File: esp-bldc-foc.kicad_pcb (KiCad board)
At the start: 4 copper layers, 92 x 92 mm, 123 parts, among them IC1 ESP32-S3FN8, IC2 LY68L6400SLIT, IC3 DRV8301DCAR, J1 USB_C_Receptacle_USB2.0, J6 Conn_01x02_Female, J7 A, J8 B, J9 C, Q1 BUK7M9R9-60EX, Q10 BUK7M9R9-60EX, Q11 BUK7M9R9-60EX, Q12 BUK7M9R9-60EX, Q2 BUK7M9R9-60EX, Q3 BUK7M9R9-60EX, Q4 BUK7M9R9-60EX, Q5 BUK7M9R9-60EX, Q6 BUK7M9R9-60EX, Q7 BUK7M9R9-60EX, Q8 BUK7M9R9-60EX, Q9 BUK7M9R9-60EX, SW1 SW_SPST, SW2 SW_SPST, U1 ADP7182AUJZ-3.3, U2 W25Q32JVZP, U3 AS5055A, U4 LMR36510ADDA, U5 LMR36510ADDA, Y1 40MHz

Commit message: finished routing
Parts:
- added J10: UART, Connector_JST:JST_PH_B3B-PH-K_1x03_P2.00mm_Vertical, F.Cu at (133.8, 90.3)
- added J2: ABZ encoder, Connector_JST:JST_PH_B5B-PH-K_1x05_P2.00mm_Vertical, F.Cu at (105.5, 107.1)
- added J3: I2C ENCODER, Connector_JST:JST_PH_B4B-PH-K_1x04_P2.00mm_Vertical, F.Cu at (103.3, 81.8)
- U3: value AS5055A -> AS5048B; footprint Package_DFN_QFN:QFN-16-1EP_4x4mm_P0.65mm_EP2.7x2.7mm_PullBack -> Package_SO:TSSOP-14_4.4x5mm_P0.65mm
- moved R13 11.4 mm to (157.5, 86.3), turned to 90 degrees
- moved C2 1.90 mm to (119.6, 82.2), turned to 0 degrees
- moved C32 1.73 mm to (141.0, 90.8)
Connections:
- IC1 pad 18: /ENC_B -> /ENC_Z
- IC1 pad 19: /ENC_Z -> /ENC_B
- IC1 pad 44: /AS5055_CS -> /ENC_PWM
- U3 pad 1: /ENC_MOSI -> /SDA
- U3 pad 14: unconnected-(U3-Pad14) -> /ENC_PWM
- U3 pad 2: /ENC_MISO -> /SCL
- U3 pad 3: /ENC_SCK -> GND
- U3 pad 4: /AS5055_CS -> GND
- U3 pad 9: GND -> unconnected-(U3-Pad9)
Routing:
- net /SDA: track 0.00 -> 55.9 mm, vias 0 -> 2
- net /SCL: track 0.00 -> 55.0 mm, vias 0 -> 2
- net /MCU/IO4: track 3.96 -> 49.6 mm, vias 0 -> 2
- net /ENC_MISO: track 4.88 -> 37.6 mm, vias 3 -> 2
- net /ENC_SCK: track 2.49 -> 33.7 mm, vias 3 -> 2
- net /MCU/IO10: track 1.94 -> 33.0 mm, vias 2 -> 3
- net /MCU/IO9: track 6.76 -> 36.9 mm
- net /MCU/IO11: track 5.49 -> 35.5 mm
- net /ENC_MOSI: track 3.48 -> 33.4 mm, vias 3 -> 2
- net /ENC_PWM: track 0.00 -> 22.4 mm, vias 0 -> 2
- net /MCU/IO5: track 1.62 -> 21.7 mm, vias 1 -> 3
- net /ENC_Z: track 0.90 -> 20.8 mm
- net /MCU/IO6: track 4.98 -> 23.6 mm, vias 1 -> 2
- net /ENC_A: track 0.71 -> 18.4 mm
- net /ENC_B: track 0.77 -> 18.4 mm
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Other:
- outline, holes or cut-outs redrawn

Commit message: Routing done
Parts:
- removed C1: C, Capacitor_SMD:C_0402_1005Metric
- removed C11: 0.1uF, Capacitor_SMD:C_0402_1005Metric
- removed C13, C15: 2200pF, Capacitor_SMD:C_0402_1005Metric
- removed C27, C39: 100nF, Capacitor_SMD:C_0402_1005Metric
- removed C30: 68uF, Capacitor_Tantalum_SMD:CP_EIA-7361-438_AVX-U_Pad2.18x3.30mm_HandSolder
- removed C31: 2.2uF, Capacitor_SMD:C_0402_1005Metric
- removed C33, C35: 220nF, Capacitor_SMD:C_0402_1005Metric
- removed C37: 1uF, Capacitor_SMD:C_0402_1005Metric
- removed C41: 10pF, Capacitor_SMD:C_0402_1005Metric
- removed C43: 47uF, Capacitor_SMD:C_1206_3216Metric
- removed C45, C48: 470uF, Capacitor_SMD:CP_Elec_10x10
- removed C50, C51: 4.7uF, Capacitor_SMD:C_1206_3216Metric
- removed D1: WS2812B, LED_SMD:LED_WS2812B_PLCC4_5.0x5.0mm_P3.2mm
- removed D4, D5: D, Diode_SMD:D_0805_2012Metric
- removed J2: ABZ encoder, Connector_JST:JST_PH_B5B-PH-K_1x05_P2.00mm_Vertical
- removed L1: L, Inductor_SMD:L_0402_1005Metric
- removed L2, L3: 22uH, Inductor_SMD:L_Bourns-SRN4018
- removed R13: 10K, Resistor_SMD:R_0402_1005Metric
- removed R14: 3.3K, Resistor_SMD:R_0402_1005Metric
- removed R23: 100K, Resistor_SMD:R_0402_1005Metric
- removed R24: 24.9K, Resistor_SMD:R_0402_1005Metric
- removed R8, R9: 22R, Resistor_SMD:R_0402_1005Metric
- removed TP1, TP2: TestPoint, TestPoint:TestPoint_Pad_D2.5mm
- removed U2: W25Q32JVZP, Package_SON:WSON-8-1EP_6x5mm_P1.27mm_EP3.4x4.3mm
- removed U4: LMR36510ADDA, Package_SO:Texas_HTSOP-8-1EP_3.9x4.9mm_P1.27mm_EP2.95x4.9mm_Mask2.4x3.1mm_ThermalVias
- R11, R12: value 120R -> 10K; footprint Resistor_SMD:R_0805_2012Metric -> Resistor_SMD:R_0402_1005Metric
- R3: value 100K -> 10K
- R4: value 18K -> 5.1K
- R5: value 3.3K -> 5.1K
- Y1: footprint Crystal:Crystal_SMD_Abracon_ABM3B-4Pin_5.0x3.2mm -> Crystal:Crystal_SMD_2016-4Pin_2.0x1.6mm
- moved C34 52.3 mm to (140.3, 113.1)
- moved R3 47.4 mm to (149.3, 77.9), turned to 180 degrees
- moved J3 38.9 mm to (137.7, 100.2), turned to -90 degrees
- moved R5 33.5 mm to (115.5, 95.1), turned to 0 degrees
- moved C49 31.4 mm to (137.9, 128.8), turned to 0 degrees
- moved R4 30.9 mm to (115.5, 94.1)
- moved C10 29.7 mm to (124.2, 107.4), turned to 180 degrees
- moved R12 26.8 mm to (140.5, 106.8), turned to -90 degrees
- moved C52 26.8 mm to (137.9, 126.3), turned to 0 degrees
- moved U1 26.1 mm to (124.7, 104.8), turned to 90 degrees
- moved R11 25.6 mm to (140.5, 103.6), turned to 90 degrees
- moved C6 20.8 mm to (124.0, 96.5), turned to 135 degrees
- moved IC2 19.9 mm to (130.5, 104.0)
- moved R2 19.9 mm to (128.8, 100.8)
- moved D6 19.8 mm to (125.6, 116.0)
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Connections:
- C25 pad 1: Net-(C25-Pad1) -> /Power_stage/SLB
- C28 pad 1: Net-(C28-Pad1) -> /Power_stage/SLC
- IC1 pad 1: Net-(C1-Pad2) -> Net-(AE1-Pad2)
- IC1 pad 23: /ENC_MOSI -> /SDA
- IC1 pad 24: /ENC_MISO -> /SCL
- IC1 pad 27: /ENC_SCK -> /MCU/IO21
- IC1 pad 44: /ENC_PWM -> /MCU/IO39
- IC1 pad 45: /ENC_CS -> /MCU/IO40
- IC1 pad 49: /MCU/TX0 -> /MCU/IO43
- IC1 pad 50: /MCU/RX0 -> /MCU/IO44
- IC1 pad 6: /SDA -> /MCU/IO1
- IC1 pad 7: /SCL -> /MCU/IO2
- IC3 pad 10: /ENC_MISO -> /MCU/IO41
- IC3 pad 11: /ENC_SCK -> /MCU/IO40
- IC3 pad 16: /MCU/IO10 -> /MCU/IO39
- IC3 pad 17: /MCU/IO33 -> /MCU/IO38
- IC3 pad 18: /MCU/IO34 -> /MCU/IO37
- IC3 pad 19: /MCU/IO35 -> /MCU/IO36
- IC3 pad 20: /MCU/IO36 -> /MCU/IO35
- IC3 pad 21: /MCU/IO37 -> /MCU/IO34
- IC3 pad 22: /MCU/IO38 -> /MCU/IO33
- IC3 pad 3: Net-(IC3-Pad3) -> unconnected-(IC3-Pad3)
- IC3 pad 31: Net-(C28-Pad1) -> /Power_stage/SLC
- IC3 pad 33: Net-(C25-Pad1) -> /Power_stage/SLB
- IC3 pad 50: Net-(C27-Pad2) -> unconnected-(IC3-Pad50)
- IC3 pad 51: Net-(C27-Pad2) -> unconnected-(IC3-Pad51)
- IC3 pad 52: Net-(C27-Pad1) -> unconnected-(IC3-Pad52)
- IC3 pad 55: unconnected-(IC3-Pad55) -> Net-(IC3-Pad55)
- IC3 pad 6: /MCU/IO9 -> /MCU/IO44
- IC3 pad 8: /MCU/IO11 -> /MCU/IO43
- IC3 pad 9: /ENC_MOSI -> /MCU/IO42
- J1 pad A5: unconnected-(J1-PadA5) -> /MCU/CC1
- J1 pad B5: unconnected-(J1-PadB5) -> /MCU/CC2
- R11 pad 1: Net-(C25-Pad1) -> /SCL
- R11 pad 2: /Power_stage/SLB -> +3.3V
- R12 pad 1: Net-(C28-Pad1) -> /SDA
- R12 pad 2: /Power_stage/SLC -> +3.3V
- R3 pad 1: /MCU/VDD_SPI -> GND
- R3 pad 2: /MCU/SPICS0 -> Net-(IC3-Pad55)
- R4 pad 1: /motor_controller/V_SENSE -> GND
- R4 pad 2: Net-(IC3-Pad3) -> /MCU/CC1
- R5 pad 1: Net-(IC3-Pad3) -> GND
- R5 pad 2: GND -> /MCU/CC2
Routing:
- net /MCU/IO4: track 49.6 -> 0.00 mm, vias 2 -> 0
- net GND: track 126.9 -> 78.4 mm, vias 584 -> 260
- net +5V: track 63.8 -> 16.9 mm, vias 5 -> 2
- net /ENC_MISO: track 37.6 -> 0.00 mm, vias 2 -> 0
- net /MCU/IO9: track 36.9 -> 0.00 mm, vias 2 -> 0
- net /MCU/IO11: track 35.5 -> 0.00 mm, vias 2 -> 0
- net /motor_controller/V_SENSE: track 34.5 -> 0.00 mm, vias 2 -> 0
- net /ENC_SCK: track 33.7 -> 0.00 mm, vias 2 -> 0
- net /ENC_MOSI: track 33.4 -> 0.00 mm, vias 2 -> 0
- net /MCU/IO10: track 33.0 -> 0.00 mm, vias 3 -> 0
- net /MCU/IO6: track 23.6 -> 0.00 mm, vias 2 -> 0
- net /MCU/SPIWP: track 32.1 -> 9.22 mm, vias 3 -> 2
- net /ENC_PWM: track 22.4 -> 0.00 mm, vias 2 -> 0
- net /SDA: track 55.9 -> 33.7 mm, vias 2 -> 1
- net /SCL: track 55.0 -> 32.9 mm, vias 2 -> 1
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- added copper zone on In1.Cu, net VBUS
- removed copper zone on B.Cu, net /Power_stage/A
- removed copper zone on In1.Cu, net /Power_stage/A
- removed copper zone on In2.Cu, net /Power_stage/A
- removed copper zone on B.Cu, net /Power_stage/B
- removed copper zone on In1.Cu, net /Power_stage/B
- removed copper zone on In2.Cu, net /Power_stage/B
- removed copper zone on B.Cu, net /Power_stage/C
- removed copper zone on In1.Cu, net /Power_stage/C
- removed copper zone on In2.Cu, net /Power_stage/C
- removed copper zone on B.Cu, net /Power_stage/SLB
- removed copper zone on B.Cu, net /Power_stage/SLC
- removed copper zone on In1.Cu, net /Power_stage/SLC
- removed copper zone on In2.Cu, net /Power_stage/SLC
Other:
- board size 92 x 92 mm -> 66 x 66 mm

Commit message: Adding more vias and clenup
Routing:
- net /MCU/VDD_SPI: track 8.46 -> 12.8 mm, vias 2 -> 4
- net +3.3V: track 39.5 -> 41.4 mm, vias 86 -> 156
- net GND: track 78.4 -> 79.2 mm, vias 260 -> 261
- net /Power_stage/A: track 27.8 -> 28.6 mm
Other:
- outline, holes or cut-outs redrawn

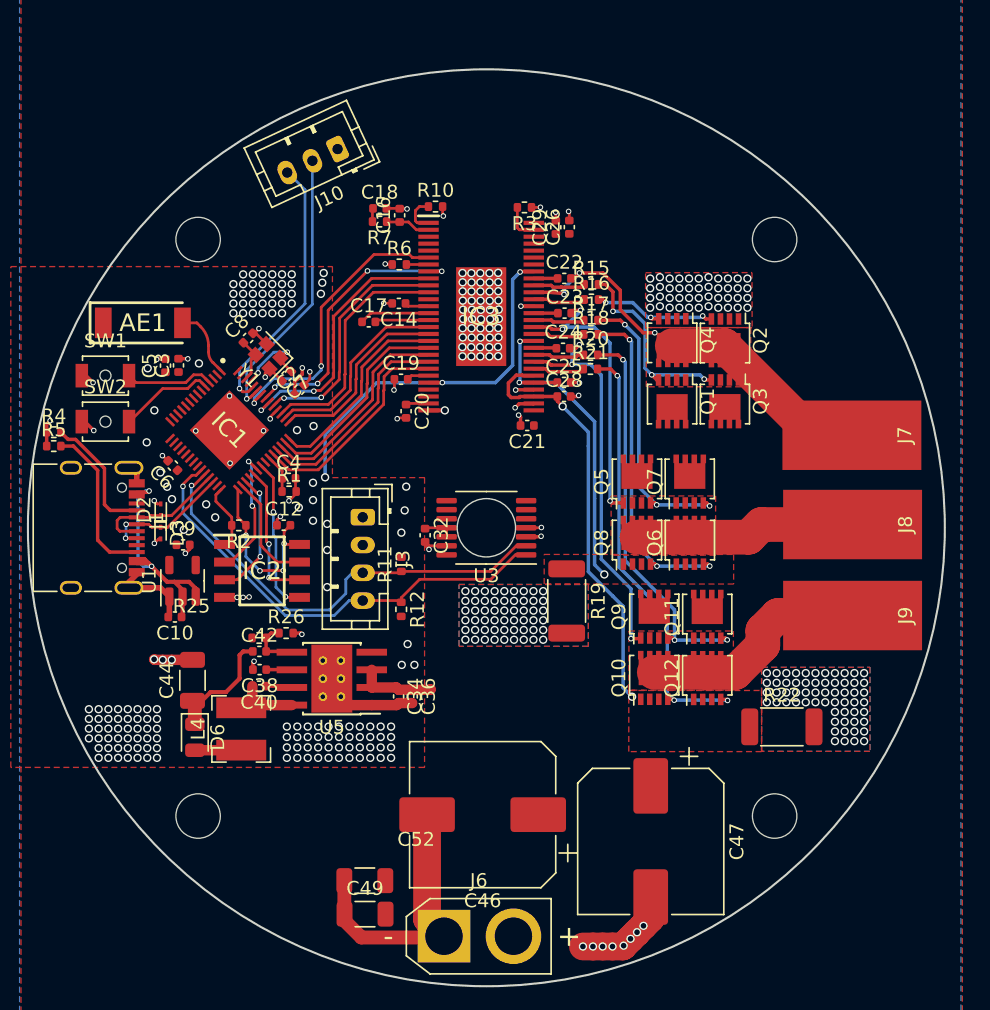
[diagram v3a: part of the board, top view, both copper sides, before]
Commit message: Adding gerber to git ignore
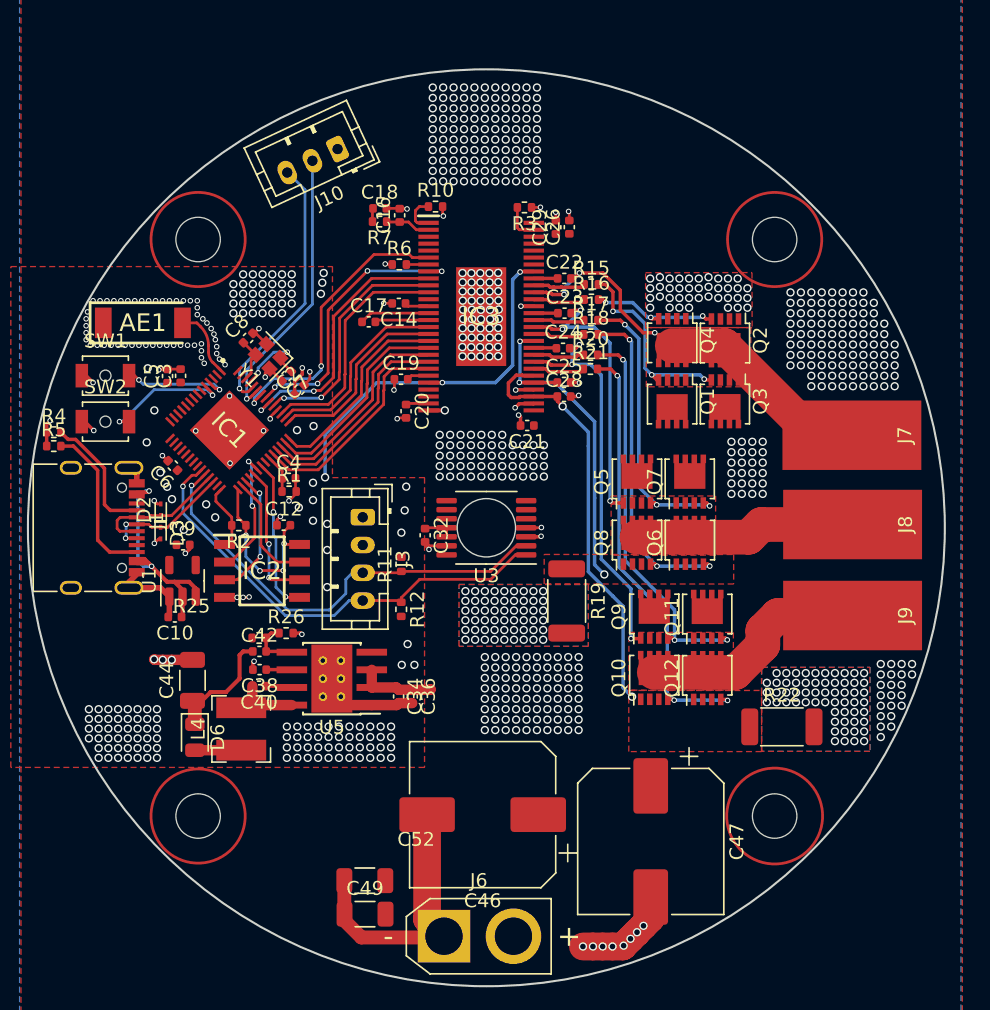
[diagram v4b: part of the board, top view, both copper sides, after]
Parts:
- moved C5 0.76 mm to (123.7, 90.0)
- moved C3 0.76 mm to (124.6, 90.0)
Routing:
- net /MCU/IO0: track 6.89 -> 9.40 mm, vias 0 -> 2
- net /MCU/RESET: track 6.45 -> 7.87 mm, vias 0 -> 2
- net GND: track 79.2 -> 79.5 mm, vias 261 -> 306
- net VBUS: vias 0 -> 384
- net +3.3V: vias 156 -> 155

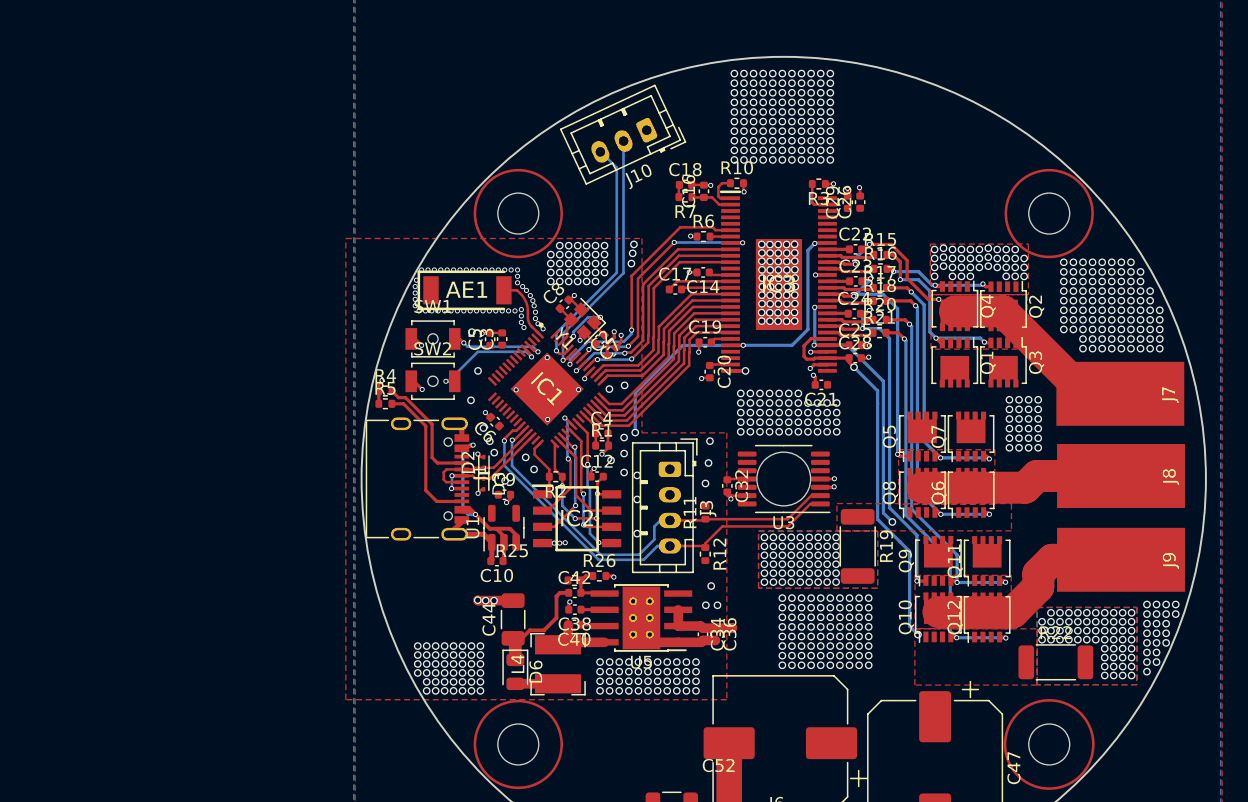
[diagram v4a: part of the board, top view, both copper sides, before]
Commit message: Using DRV8353 with built in current sense
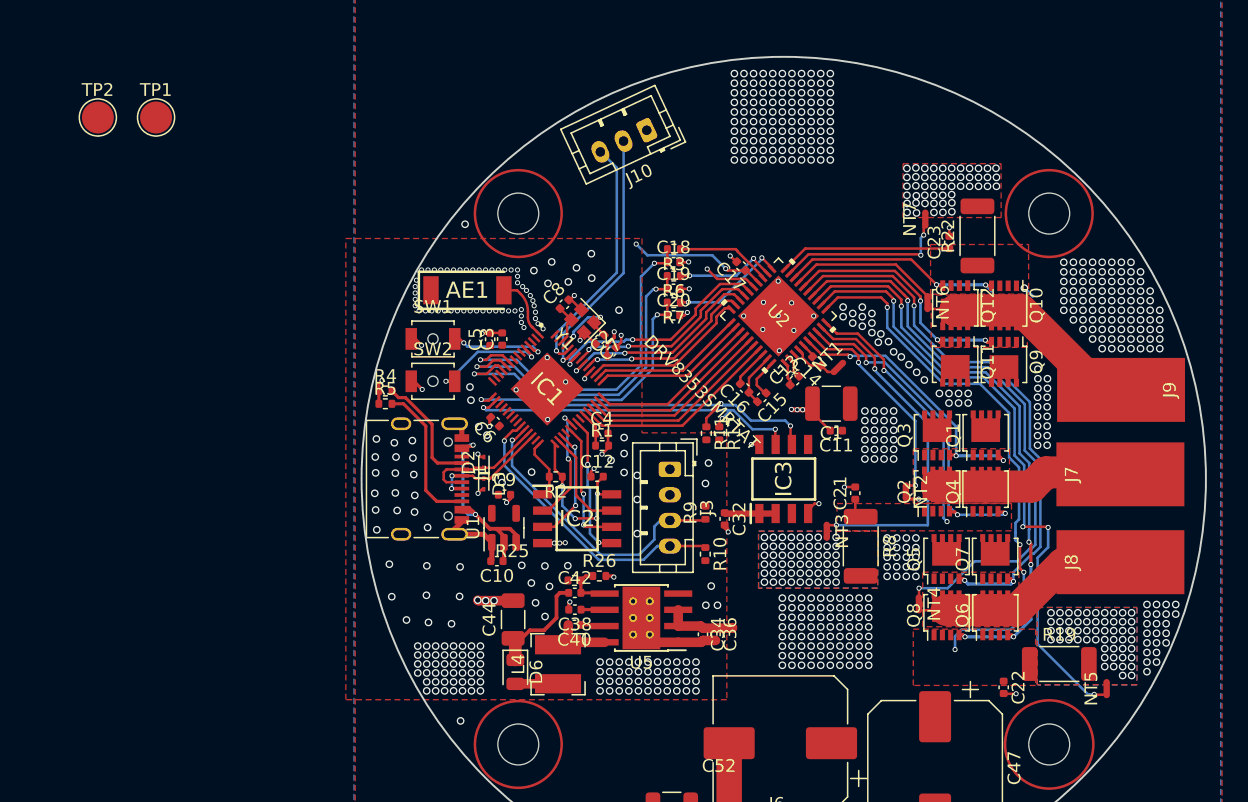
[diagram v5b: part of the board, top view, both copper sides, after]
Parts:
- removed C24: 100nF, Capacitor_SMD:C_0402_1005Metric
- removed C25, C28: 2200pF, Capacitor_SMD:C_0402_1005Metric
- removed C26: 68nF, Capacitor_SMD:C_0402_1005Metric
- removed C29: 4.7uF, Capacitor_SMD:C_0402_1005Metric
- removed R15, R16, R17, R18, R20, R21: 2.2R, Resistor_SMD:R_0402_1005Metric
- removed U3: AS5048B, Package_SO:TSSOP-14_4.4x5mm_P0.65mm
- added C1: 10uF, Capacitor_SMD:C_1210_3225Metric, F.Cu at (150.3, 95.0)
- added C11: 0.1uF, Capacitor_SMD:C_0402_1005Metric, F.Cu at (150.7, 97.2)
- added C13: 0.047uF, Capacitor_SMD:C_0402_1005Metric, F.Cu at (147.4, 93.2)
- added C15: 1uF, Capacitor_SMD:C_0402_1005Metric, F.Cu at (144.9, 94.6)
- added NT1: NetTie_2, NetTie:NetTie-2_SMD_Pad0.5mm, F.Cu at (150.9, 92.2)
- added NT2: NetTie_2, NetTie:NetTie-2_SMD_Pad0.5mm, F.Cu at (156.2, 102.0)
- added NT3: NetTie_2, NetTie:NetTie-2_SMD_Pad0.5mm, F.Cu at (150.0, 105.0)
- added NT4: NetTie_2, NetTie:NetTie-2_SMD_Pad0.5mm, F.Cu at (157.2, 110.7)
- added NT5: NetTie_2, NetTie:NetTie-2_SMD_Pad0.5mm, F.Cu at (171.8, 117.3)
- added NT6: NetTie_2, NetTie:NetTie-2_SMD_Pad0.5mm, F.Cu at (157.8, 87.2)
- added NT7: NetTie_2, NetTie:NetTie-2_SMD_Pad0.5mm, F.Cu at (157.7, 80.6)
- added R8: 500u, Resistor_SMD:R_2010_5025Metric, F.Cu at (152.6, 106.2)
- added R9: 10K, Resistor_SMD:R_0402_1005Metric, F.Cu at (140.5, 103.6)
- added TP1: TestPoint, TestPoint:TestPoint_Pad_D2.5mm, F.Cu at (97.5, 72.7)
- added TP2: TestPoint, TestPoint:TestPoint_Pad_D2.5mm, F.Cu at (93.0, 72.7)
- added U2: DRV8353SMRTAT, DRV8353M:DRV8353SMRTAT, F.Cu at (146.2, 88.2)
- C14: value 2.2uF -> 1uF
- C16: value 82pF -> 1uF
- C17: value 22nF -> 0.1uF
- C18: value 270pF -> 2200pF
- C19, C20: value 2.2uF -> 2200pF
- C21: value 68nF -> 1000pF
- C22, C23: value 100nF -> 1000pF
- IC3: value DRV8301DCAR -> AS5600-ASOM; footprint DRV8301:SOP50P810X120-57N -> AS5600:SOIC127P600X175-8N
- R10: value 220K -> 10K
- R3: value 10K -> 56R
- R6: value 18K -> 56R
- R7: value 47K -> 56R
- moved C22 36.1 mm to (163.8, 117.2), turned to -90 degrees
- moved R22 33.9 mm to (161.7, 81.9), turned to 90 degrees
- moved R10 29.1 mm to (140.5, 106.8), turned to -90 degrees
- moved Q10 24.9 mm to (163.8, 87.4), turned to -90 degrees
- moved Q12 24.5 mm to (160.0, 87.4), turned to -90 degrees
- moved R19 18.2 mm to (168.2, 115.4), turned to 0 degrees
- moved Q9 16.4 mm to (163.8, 91.8), turned to -90 degrees
- moved Q11 15.8 mm to (160.0, 91.8), turned to -90 degrees
- moved C16 15.7 mm to (143.6, 93.8), turned to 135 degrees
- moved Q2 15.4 mm to (158.6, 101.9), turned to 90 degrees
- moved IC3 15.2 mm to (146.6, 100.9), turned to 90 degrees
- moved Q4 14.7 mm to (162.4, 101.9), turned to 90 degrees
- moved J9 13.3 mm to (173.0, 94.0)
- moved R3 12.4 mm to (138.0, 83.0)
- moved C14 11.3 mm to (149.2, 91.7), turned to 135 degrees
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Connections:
- net /ENC_A renamed /MCU/IO12
- net /ENC_B renamed /MCU/IO14
- net /ENC_Z renamed /MCU/IO13
- C14 pad 1: Net-(C14-Pad1) -> /motor_controller/VDRAIN
- C14 pad 2: GND -> Net-(C14-Pad2)
- C16 pad 1: Net-(C16-Pad1) -> Net-(C15-Pad2)
- C16 pad 2: GND -> Net-(C16-Pad2)
- C17 pad 1: Net-(C17-Pad1) -> +3.3V
- C17 pad 2: Net-(C17-Pad2) -> GND
- C18 pad 1: Net-(C18-Pad1) -> /MCU/IO4
- C19 pad 1: GND -> /MCU/IO5
- C19 pad 2: Net-(C19-Pad2) -> GND
- C20 pad 1: Net-(C20-Pad1) -> /MCU/IO6
- C21 pad 1: VBUS -> /Power_stage/SN1
- C22 pad 1: Net-(C22-Pad1) -> /Power_stage/SN2
- C22 pad 2: /Power_stage/A -> GND
- C23 pad 1: Net-(C23-Pad1) -> /Power_stage/SN3
- C23 pad 2: /Power_stage/B -> GND
- IC1 pad 15: /MCU/IO10 -> /SCL
- IC1 pad 16: /MCU/IO11 -> /SDA
- IC1 pad 23: /SDA -> /EXT_SDA
- IC1 pad 24: /SCL -> /EXT_SCL
- IC3 pad 1: Net-(IC3-Pad1) -> +3.3V
- IC3 pad 2: Net-(C16-Pad1) -> +3.3V
- IC3 pad 4: unconnected-(IC3-Pad4) -> GND
- IC3 pad 5: /motor_controller/nOCTW -> unconnected-(IC3-Pad5)
- IC3 pad 6: /MCU/IO44 -> /SCL
- IC3 pad 7: Net-(IC3-Pad7) -> /SDA
- IC3 pad 8: /MCU/IO43 -> GND
- J3 pad 3: /SCL -> /EXT_SCL
- J3 pad 4: /SDA -> /EXT_SDA
- Q1 pad 4: Net-(Q1-Pad4) -> /Power_stage/GHA
- Q10 pad 1: /Power_stage/SLC -> /Power_stage/SN3
- Q10 pad 2: /Power_stage/SLC -> /Power_stage/SN3
- Q10 pad 3: /Power_stage/SLC -> /Power_stage/SN3
- Q10 pad 4: Net-(Q10-Pad4) -> /Power_stage/GLC
- Q11 pad 4: Net-(Q11-Pad4) -> /Power_stage/GHC
- Q12 pad 1: /Power_stage/SLC -> /Power_stage/SN3
- Q12 pad 2: /Power_stage/SLC -> /Power_stage/SN3
- Q12 pad 3: /Power_stage/SLC -> /Power_stage/SN3
- Q12 pad 4: Net-(Q10-Pad4) -> /Power_stage/GLC
- Q2 pad 1: GND -> /Power_stage/SN1
- Q2 pad 2: GND -> /Power_stage/SN1
- Q2 pad 3: GND -> /Power_stage/SN1
- Q2 pad 4: Net-(Q2-Pad4) -> /Power_stage/GLA
- Q3 pad 4: Net-(Q1-Pad4) -> /Power_stage/GHA
- Q4 pad 1: GND -> /Power_stage/SN1
- Q4 pad 2: GND -> /Power_stage/SN1
- Q4 pad 3: GND -> /Power_stage/SN1
- Q4 pad 4: Net-(Q2-Pad4) -> /Power_stage/GLA
- Q5 pad 4: Net-(Q5-Pad4) -> /Power_stage/GHB
- Q6 pad 1: /Power_stage/SLB -> /Power_stage/SN2
- Q6 pad 2: /Power_stage/SLB -> /Power_stage/SN2
- Q6 pad 3: /Power_stage/SLB -> /Power_stage/SN2
- Q6 pad 4: Net-(Q6-Pad4) -> /Power_stage/GLB
- Q7 pad 4: Net-(Q5-Pad4) -> /Power_stage/GHB
- Q8 pad 1: /Power_stage/SLB -> /Power_stage/SN2
- Q8 pad 2: /Power_stage/SLB -> /Power_stage/SN2
- Q8 pad 3: /Power_stage/SLB -> /Power_stage/SN2
- Q8 pad 4: Net-(Q6-Pad4) -> /Power_stage/GLB
- Q9 pad 4: Net-(Q11-Pad4) -> /Power_stage/GHC
- R10 pad 1: Net-(IC3-Pad1) -> /EXT_SDA
- R10 pad 2: GND -> +3.3V
- R19 pad 1: /Power_stage/SLB -> /Power_stage/SN2
- R22 pad 1: /Power_stage/SLC -> /Power_stage/SN3
- R3 pad 1: GND -> Net-(R3-Pad1)
- R3 pad 2: Net-(IC3-Pad55) -> /MCU/IO4
- R6 pad 1: GND -> Net-(R6-Pad1)
- R6 pad 2: Net-(IC3-Pad7) -> /MCU/IO5
- R7 pad 1: Net-(C16-Pad1) -> Net-(R7-Pad1)
- R7 pad 2: Net-(C18-Pad1) -> /MCU/IO6
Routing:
- net /Power_stage/SP2: track 0.00 -> 48.5 mm, vias 0 -> 4
- net /Power_stage/SHB: track 0.00 -> 44.9 mm, vias 0 -> 2
- net /Power_stage/SN2: track 0.00 -> 43.2 mm, vias 0 -> 4
- net /Power_stage/GLB: track 3.74 -> 45.2 mm, vias 0 -> 5
- net /Power_stage/GHB: track 3.70 -> 43.7 mm, vias 0 -> 3
- net Net-(Q10-Pad4): track 31.5 -> 0.00 mm, vias 3 -> 0
- net /Power_stage/SLC: track 30.4 -> 0.00 mm, vias 2 -> 0
- net Net-(Q11-Pad4): track 28.6 -> 0.00 mm, vias 3 -> 0
- net /Power_stage/SP1: track 0.00 -> 27.9 mm, vias 0 -> 2
- net /MCU/IO4: track 0.00 -> 27.5 mm, vias 0 -> 2
- net /Power_stage/C: track 44.9 -> 17.7 mm, vias 3 -> 0
- net /MCU/IO5: track 0.00 -> 26.2 mm, vias 0 -> 2
- net /MCU/IO6: track 0.00 -> 24.7 mm, vias 0 -> 2
- net /Power_stage/SLB: track 24.6 -> 0.00 mm, vias 3 -> 0
- net Net-(Q6-Pad4): track 24.4 -> 0.00 mm, vias 3 -> 0
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- added copper zone on F.Cu, net /Power_stage/SN1
- added copper zone on In1.Cu, net /Power_stage/SN1
- added copper zone on In2.Cu, net /Power_stage/SN1
- added copper zone on F.Cu, net /Power_stage/SN2
- added copper zone on F.Cu, net /Power_stage/SN3
- removed copper zone on F.Cu, net /Power_stage/SLB
- removed copper zone on In1.Cu, net /Power_stage/SLB
- removed copper zone on In2.Cu, net /Power_stage/SLB
- removed copper zone on F.Cu, net /Power_stage/SLC
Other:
- outline, holes or cut-outs redrawn
